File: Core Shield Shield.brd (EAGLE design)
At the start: 68.6 x 53.3 mm, 10 parts, among them IC1 MC33269T-5.0

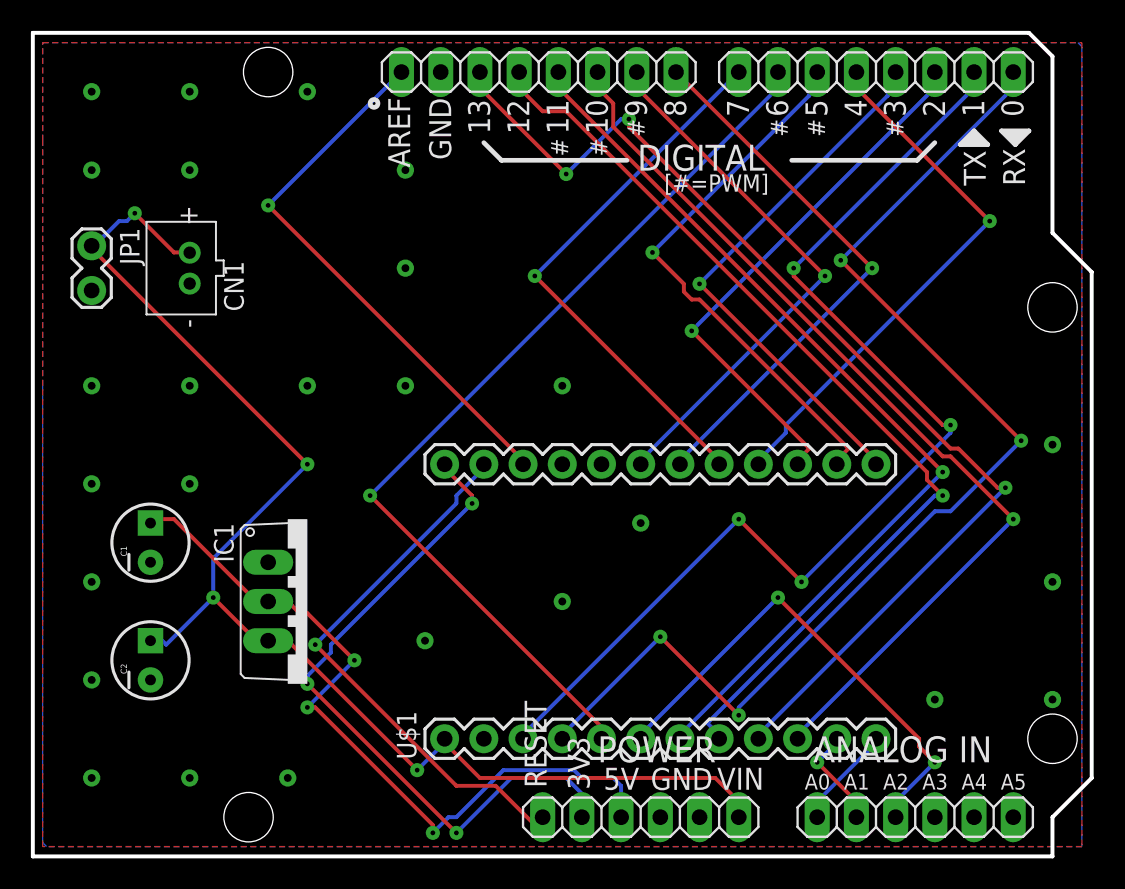
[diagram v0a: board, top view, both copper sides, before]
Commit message: Re-routed traces
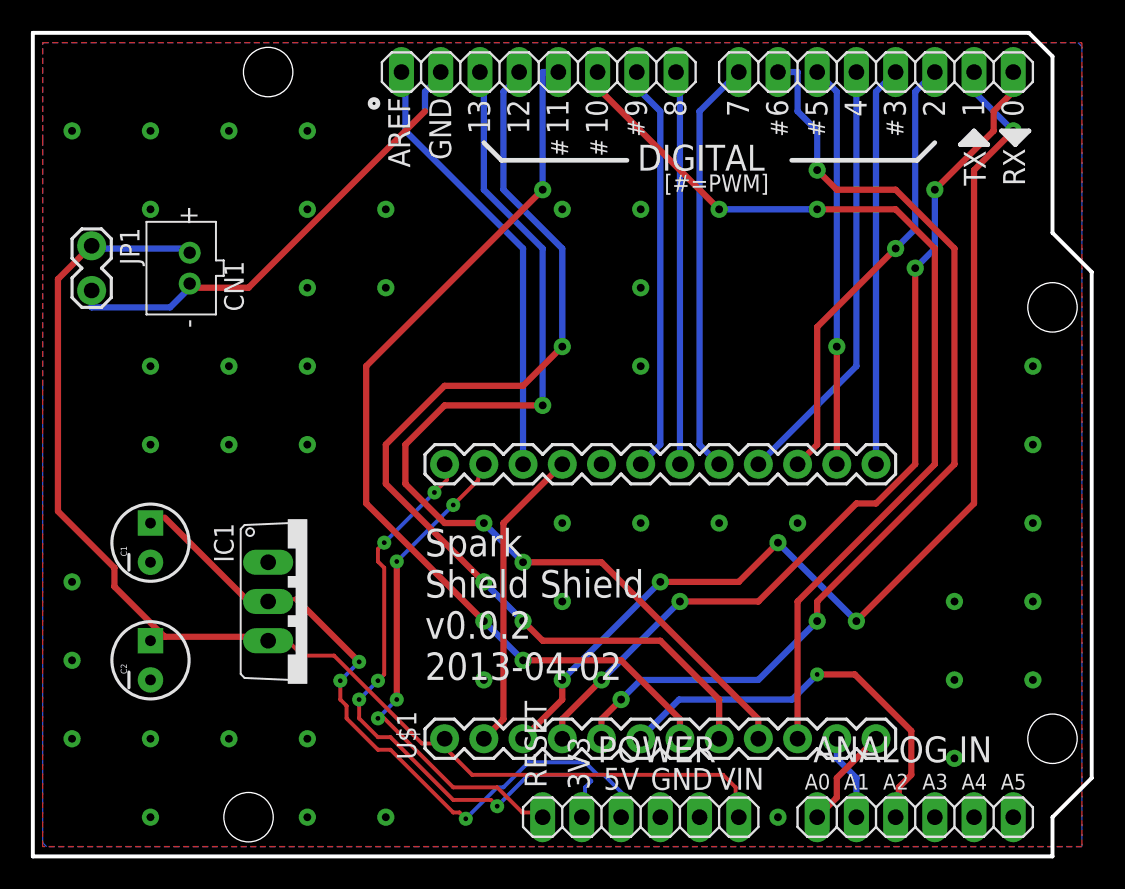
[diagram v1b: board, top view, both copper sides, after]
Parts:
- added U$2: (no value), Spark:SPARK_LOGO
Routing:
- net GND: track 0.00 -> 51.9 mm, vias 0 -> 43
- net IO0: track 76.1 -> 59.0 mm
- net IO8: track 36.2 -> 25.7 mm, vias 1 -> 0
- net VIN: track 90.9 -> 80.4 mm, vias 4 -> 0
- net IO5: track 35.8 -> 25.9 mm
- net IO3: track 35.8 -> 25.9 mm, vias 1 -> 0
- net IO7: track 36.2 -> 27.0 mm, vias 1 -> 0
- net IO9: track 35.8 -> 26.7 mm, vias 1 -> 0
- net IO4: track 35.5 -> 28.0 mm, vias 1 -> 0
- net AREF: track 36.2 -> 28.8 mm, vias 1 -> 0
- net IO2: track 35.5 -> 29.1 mm
- net SCK: track 72.3 -> 66.3 mm
- net AD2: track 32.7 -> 26.8 mm, vias 2 -> 1
- net +3V3: track 44.9 -> 40.2 mm, vias 3 -> 5
- net MISO: track 62.5 -> 66.7 mm, vias 1 -> 3
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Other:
- board text added: "Spark Shield Shield v0.0.2 2013-04-02"
